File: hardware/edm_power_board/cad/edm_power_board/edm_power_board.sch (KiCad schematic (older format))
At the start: 0 parts

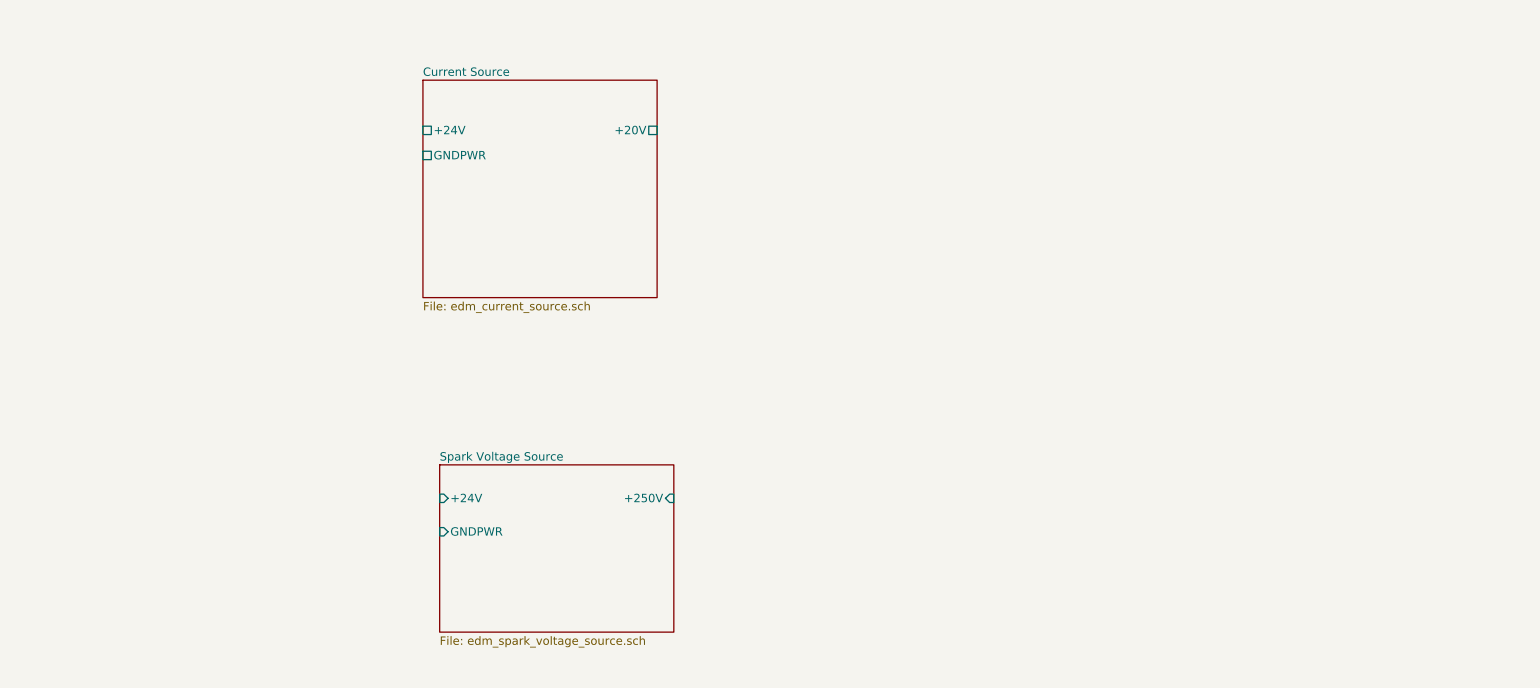
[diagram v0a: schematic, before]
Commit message: Spark voltage source
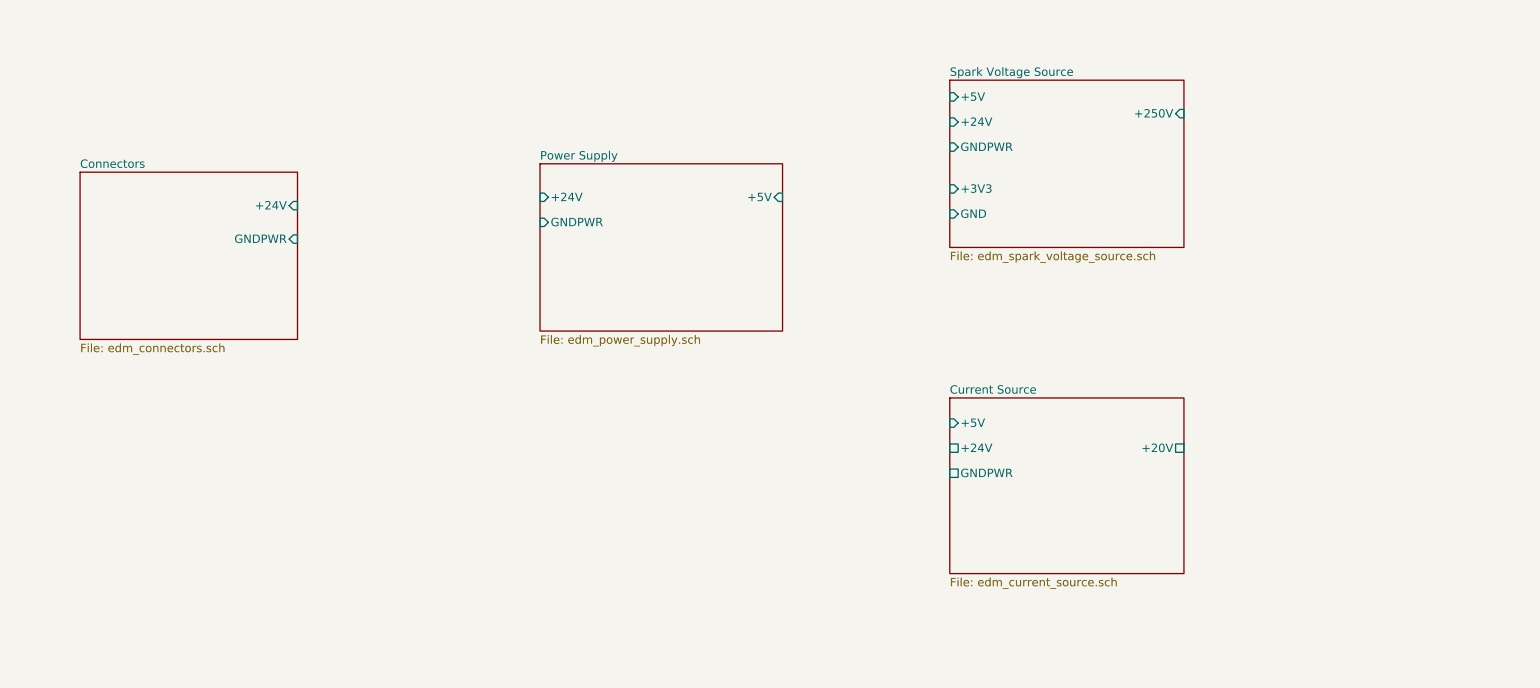
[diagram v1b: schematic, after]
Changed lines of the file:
@@
 $Descr A4 11693 8268
 encoding utf-8
-Sheet 1 3
+Sheet 1 5
 Title ""
 Date ""
@@
 $EndDescr
 $Sheet
-S 3650 2000 1400 1300
+S 6800 3900 1400 1050
 U 5A71F0AB
 F0 "Current Source" 50
 F1 "edm_current_source.sch" 50
-F2 "+24V" U L 3650 2300 50
-F3 "GNDPWR" U L 3650 2450 50
-F4 "+20V" U R 5050 2300 50
+F2 "+24V" U L 6800 4200 50
+F3 "GNDPWR" U L 6800 4350 50
+F4 "+20V" U R 8200 4200 50
+F5 "+5V" I L 6800 4050 50
 $EndSheet
 $Sheet
-S 3750 4300 1400 1000
+S 6800 2000 1400 1000
 U 5A728D61
 F0 "Spark Voltage Source" 50
 F1 "edm_spark_voltage_source.sch" 50
-F2 "+24V" I L 3750 4500 50
-F3 "GNDPWR" I L 3750 4700 50
-F4 "+250V" I R 5150 4500 50
+F2 "+24V" I L 6800 2250 50
+F3 "GNDPWR" I L 6800 2400 50
+F4 "+250V" I R 8200 2200 50
+F5 "+5V" I L 6800 2100 50
+F6 "GND" I L 6800 2800 50
+F7 "+3V3" I L 6800 2650 50
+$EndSheet
+$Sheet
+S 4350 2500 1450 1000
+U 5A73A880
+F0 "Power Supply" 50
+F1 "edm_power_supply.sch" 50
+F2 "+24V" I L 4350 2700 50
+F3 "GNDPWR" I L 4350 2850 50
+F4 "+5V" I R 5800 2700 50
+$EndSheet
+$Sheet
+S 1600 2550 1300 1000
+U 5A73A88E
+F0 "Connectors" 50
+F1 "edm_connectors.sch" 50
+F2 "+24V" I R 2900 2750 50
+F3 "GNDPWR" I R 2900 2950 50
 $EndSheet
 $EndSCHEMATC

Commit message: Insulator
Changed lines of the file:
@@
 $Descr A4 11693 8268
 encoding utf-8
-Sheet 1 5
+Sheet 1 6
 Title ""
 Date ""
@@
 $EndDescr
 $Sheet
-S 6800 3900 1400 1050
+S 5000 3750 1400 400
 U 5A71F0AB
 F0 "Current Source" 50
 F1 "edm_current_source.sch" 50
-F2 "+24V" U L 6800 4200 50
-F3 "GNDPWR" U L 6800 4350 50
-F4 "+20V" U R 8200 4200 50
-F5 "+5V" I L 6800 4050 50
+F2 "+24V" U L 5000 3950 50
+F3 "GNDPWR" U L 5000 4050 50
+F4 "+20V" U R 6400 3850 50
+F5 "+5V" I L 5000 3850 50
 $EndSheet
 $Sheet
-S 6800 2000 1400 1000
+S 5000 2700 1400 600
 U 5A728D61
 F0 "Spark Voltage Source" 50
 F1 "edm_spark_voltage_source.sch" 50
-F2 "+24V" I L 6800 2250 50
-F3 "GNDPWR" I L 6800 2400 50
-F4 "+250V" I R 8200 2200 50
-F5 "+5V" I L 6800 2100 50
-F6 "GND" I L 6800 2800 50
-F7 "+3V3" I L 6800 2650 50
+F2 "+24V" I L 5000 2900 50
+F3 "GNDPWR" I L 5000 3000 50
+F4 "+250V" I R 6400 2800 50
+F5 "+5V" I L 5000 2800 50
+F6 "GND" I L 5000 3200 50
+F7 "+3V3" I L 5000 3100 50
+F8 "Spark_Voltage_0" I R 6400 2900 50
+F9 "Spark_Voltage_1" I R 6400 3000 50
+F10 "Spark_Voltage_2" I R 6400 3100 50
+F11 "Spark_Voltage_Status" I R 6400 3200 50
 $EndSheet
 $Sheet
-S 4350 2500 1450 1000
+S 2900 2700 1200 1000
 U 5A73A880
 F0 "Power Supply" 50
 F1 "edm_power_supply.sch" 50
-F2 "+24V" I L 4350 2700 50
-F3 "GNDPWR" I L 4350 2850 50
-F4 "+5V" I R 5800 2700 50
+F2 "+24V" I L 2900 2900 50
+F3 "GNDPWR" I L 2900 3050 50
+F4 "+5V" I R 4100 2900 50
 $EndSheet
 $Sheet
-S 1600 2550 1300 1000
+S 1200 2700 1200 1000
 U 5A73A88E
 F0 "Connectors" 50
 F1 "edm_connectors.sch" 50
-F2 "+24V" I R 2900 2750 50
-F3 "GNDPWR" I R 2900 2950 50
+F2 "+24V" I R 2400 2900 50
+F3 "GNDPWR" I R 2400 3100 50
+$EndSheet
+$Sheet
+S 7550 2650 1300 800
+U 5A9693D9
+F0 "Spark Output" 50
+F1 "edm_spark_output.sch" 50
 $EndSheet
 $EndSCHEMATC

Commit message: Interconnections
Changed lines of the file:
@@
 $EndDescr
 $Sheet
-S 5000 3750 1400 400
+S 5050 5050 1400 400
 U 5A71F0AB
 F0 "Current Source" 50
 F1 "edm_current_source.sch" 50
-F2 "+24V" U L 5000 3950 50
-F3 "GNDPWR" U L 5000 4050 50
-F4 "+20V" U R 6400 3850 50
-F5 "+5V" I L 5000 3850 50
-$EndSheet
-$Sheet
-S 5000 2700 1400 600
+F2 "+24V" U L 5050 5250 50
+F3 "GNDPWR" U L 5050 5350 50
+F4 "+20V" U R 6450 5150 50
+F5 "+5V" I L 5050 5150 50
+$EndSheet
+$Sheet
+S 5050 3550 1400 600
 U 5A728D61
 F0 "Spark Voltage Source" 50
 F1 "edm_spark_voltage_source.sch" 50
-F2 "+24V" I L 5000 2900 50
-F3 "GNDPWR" I L 5000 3000 50
-F4 "+250V" I R 6400 2800 50
-F5 "+5V" I L 5000 2800 50
-F6 "GND" I L 5000 3200 50
-F7 "+3V3" I L 5000 3100 50
-F8 "Spark_Voltage_0" I R 6400 2900 50
-F9 "Spark_Voltage_1" I R 6400 3000 50
-F10 "Spark_Voltage_2" I R 6400 3100 50
-F11 "Spark_Voltage_Status" I R 6400 3200 50
-$EndSheet
-$Sheet
-S 2900 2700 1200 1000
+F2 "+24V" I L 5050 3750 50
+F3 "GNDPWR" I L 5050 3850 50
+F4 "+250V" I R 6450 3650 50
+F5 "+5V" I L 5050 3650 50
+F6 "GND" I L 5050 4050 50
+F7 "+3V3" I L 5050 3950 50
+F8 "Spark_Voltage_0" I R 6450 3750 50
+F9 "Spark_Voltage_1" I R 6450 3850 50
+F10 "Spark_Voltage_2" I R 6450 3950 50
+F11 "Spark_Voltage_Status" I R 6450 4050 50
+$EndSheet
+$Sheet
+S 1950 3550 1400 750
 U 5A73A880
 F0 "Power Supply" 50
 F1 "edm_power_supply.sch" 50
-F2 "+24V" I L 2900 2900 50
-F3 "GNDPWR" I L 2900 3050 50
-F4 "+5V" I R 4100 2900 50
-$EndSheet
-$Sheet
-S 1200 2700 1200 1000
+F2 "+24V" I L 1950 3650 50
+F3 "GNDPWR" I L 1950 3750 50
+F4 "+5V" I R 3350 3650 50
+$EndSheet
+$Sheet
+S 5050 1700 1400 900
 U 5A73A88E
 F0 "Connectors" 50
 F1 "edm_connectors.sch" 50
-F2 "+24V" I R 2400 2900 50
-F3 "GNDPWR" I R 2400 3100 50
-$EndSheet
-$Sheet
-S 7550 2650 1300 800
+F2 "+24V" I L 5050 1800 50
+F3 "GNDPWR" I L 5050 1900 50
+F4 "Output_250V_Enable" I R 6450 1800 50
+F5 "Output_20V_Enable" I R 6450 1900 50
+F6 "Short_Circuit" I R 6450 2000 50
+F7 "Breakdown" I R 6450 2100 50
+F8 "Spark_Voltage_0" I R 6450 2200 50
+F9 "Spark_Voltage_1" I R 6450 2300 50
+F10 "Spark_Voltage_2" I R 6450 2400 50
+F11 "Spark_Voltage_Status" I R 6450 2500 50
+F12 "+3V3" I L 5050 2100 50
+F13 "GND" I L 5050 2200 50
+$EndSheet
+$Sheet
+S 8250 3550 1300 700
 U 5A9693D9
 F0 "Spark Output" 50
 F1 "edm_spark_output.sch" 50
-$EndSheet
+F2 "+250V" I L 8250 3650 50
+F3 "+20V" I L 8250 3750 50
+F4 "+5V" I L 8250 4050 50
+F5 "+3V3" I L 8250 3850 50
+F6 "GND" I L 8250 3950 50
+F7 "GNDPWR" I L 8250 4150 50
+F8 "Output_250V_Enable" I R 9550 3650 50
+F9 "Output_20V_Enable" I R 9550 3750 50
+F10 "Short_Circuit" I R 9550 3850 50
+F11 "Breakdown" I R 9550 3950 50
+$EndSheet
+Wire Wire Line
+	6450 3650 8250 3650
+Wire Wire Line
+	6450 5150 7400 5150
+Wire Wire Line
+	7400 5150 7400 3750
+Wire Wire Line
+	7400 3750 8250 3750
+Wire Wire Line
+	6450 3750 6700 3750
+Wire Wire Line
+	6700 3750 6700 2200
+Wire Wire Line
+	6700 2200 6450 2200
+Wire Wire Line
+	6450 2300 6800 2300
+Wire Wire Line
+	6800 2300 6800 3850
+Wire Wire Line
+	6800 3850 6450 3850
+Wire Wire Line
+	6450 3950 6900 3950
+Wire Wire Line
+	6900 3950 6900 2400
+Wire Wire Line
+	6900 2400 6450 2400
+Wire Wire Line
+	6450 2500 7000 2500
+Wire Wire Line
+	7000 2500 7000 4050
+Wire Wire Line
+	7000 4050 6450 4050
+Wire Wire Line
+	6450 2100 10200 2100
+Wire Wire Line
+	10200 2100 10200 3950
+Wire Wire Line
+	10200 3950 9550 3950
+Wire Wire Line
+	6450 2000 10100 2000
+Wire Wire Line
+	10100 2000 10100 3850
+Wire Wire Line
+	10100 3850 9550 3850
+Wire Wire Line
+	9550 3750 10000 3750
+Wire Wire Line
+	10000 3750 10000 1900
+Wire Wire Line
+	10000 1900 6450 1900
+Wire Wire Line
+	6450 1800 9900 1800
+Wire Wire Line
+	9900 1800 9900 3650
+Wire Wire Line
+	9900 3650 9550 3650
+Wire Wire Line
+	3350 3650 4150 3650
+Wire Wire Line
+	5050 5150 4700 5150
+Wire Wire Line
+	4150 5150 4150 3650
+Connection ~ 4150 3650
+Wire Wire Line
+	4150 3650 5050 3650
+Wire Wire Line
+	5050 5250 4250 5250
+Wire Wire Line
+	4250 5250 4250 3750
+Wire Wire Line
+	4250 3750 5050 3750
+Wire Wire Line
+	5050 3850 4350 3850
+Wire Wire Line
+	4350 3850 4350 5350
+Wire Wire Line
+	4350 5350 4800 5350
+Wire Wire Line
+	5050 3950 4600 3950
+Wire Wire Line
+	4600 3950 4600 2100
+Wire Wire Line
+	4600 2100 5050 2100
+Wire Wire Line
+	5050 4050 4700 4050
+Wire Wire Line
+	4700 4050 4700 2200
+Wire Wire Line
+	4700 2200 5050 2200
+Wire Wire Line
+	7750 4450 4600 4450
+Wire Wire Line
+	4600 4450 4600 3950
+Connection ~ 4600 3950
+Wire Wire Line
+	7850 4550 4700 4550
+Wire Wire Line
+	4700 4550 4700 4050
+Connection ~ 4700 4050
+Wire Wire Line
+	4350 5350 1700 5350
+Wire Wire Line
+	1700 5350 1700 3750
+Wire Wire Line
+	1700 3750 1950 3750
+Connection ~ 4350 5350
+Wire Wire Line
+	1950 3650 1600 3650
+Wire Wire Line
+	1600 3650 1600 5250
+Wire Wire Line
+	1600 5250 4250 5250
+Connection ~ 4250 5250
+Wire Wire Line
+	4800 5350 4800 4750
+Connection ~ 4800 5350
+Wire Wire Line
+	4800 5350 5050 5350
+Wire Wire Line
+	4700 4650 4700 5150
+Connection ~ 4700 5150
+Wire Wire Line
+	4700 5150 4150 5150
+Wire Wire Line
+	7750 4450 7750 3850
+Wire Wire Line
+	7750 3850 8250 3850
+Wire Wire Line
+	8250 3950 7850 3950
+Wire Wire Line
+	7850 3950 7850 4550
+Wire Wire Line
+	8250 4050 7950 4050
+Wire Wire Line
+	7950 4050 7950 4650
+Wire Wire Line
+	4700 4650 7950 4650
+Wire Wire Line
+	8050 4750 8050 4150
+Wire Wire Line
+	8050 4150 8250 4150
+Wire Wire Line
+	4800 4750 8050 4750
+Wire Wire Line
+	1700 3750 1700 1900
+Wire Wire Line
+	1700 1900 5050 1900
+Connection ~ 1700 3750
+Wire Wire Line
+	5050 1800 1600 1800
+Wire Wire Line
+	1600 1800 1600 3650
+Connection ~ 1600 3650
 $EndSCHEMATC

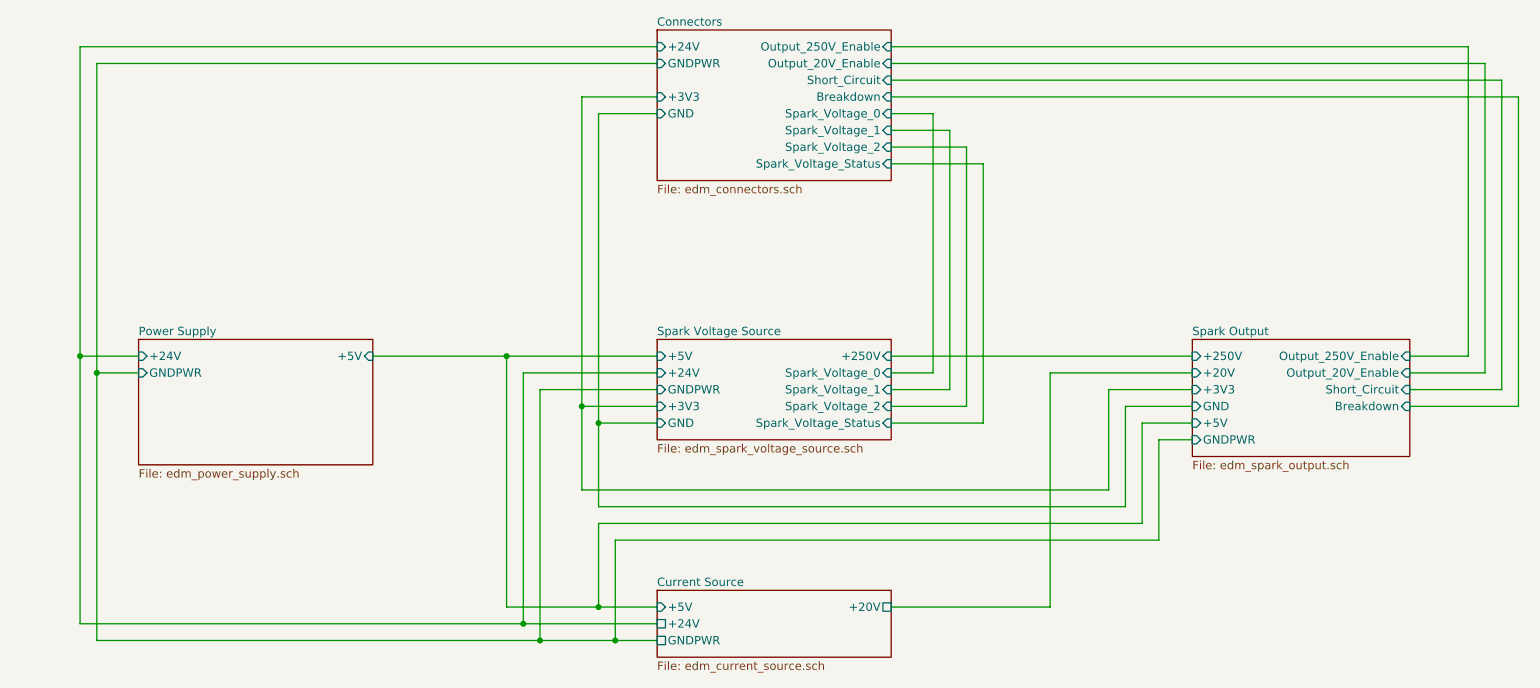
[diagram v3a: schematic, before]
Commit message: Spark output connector
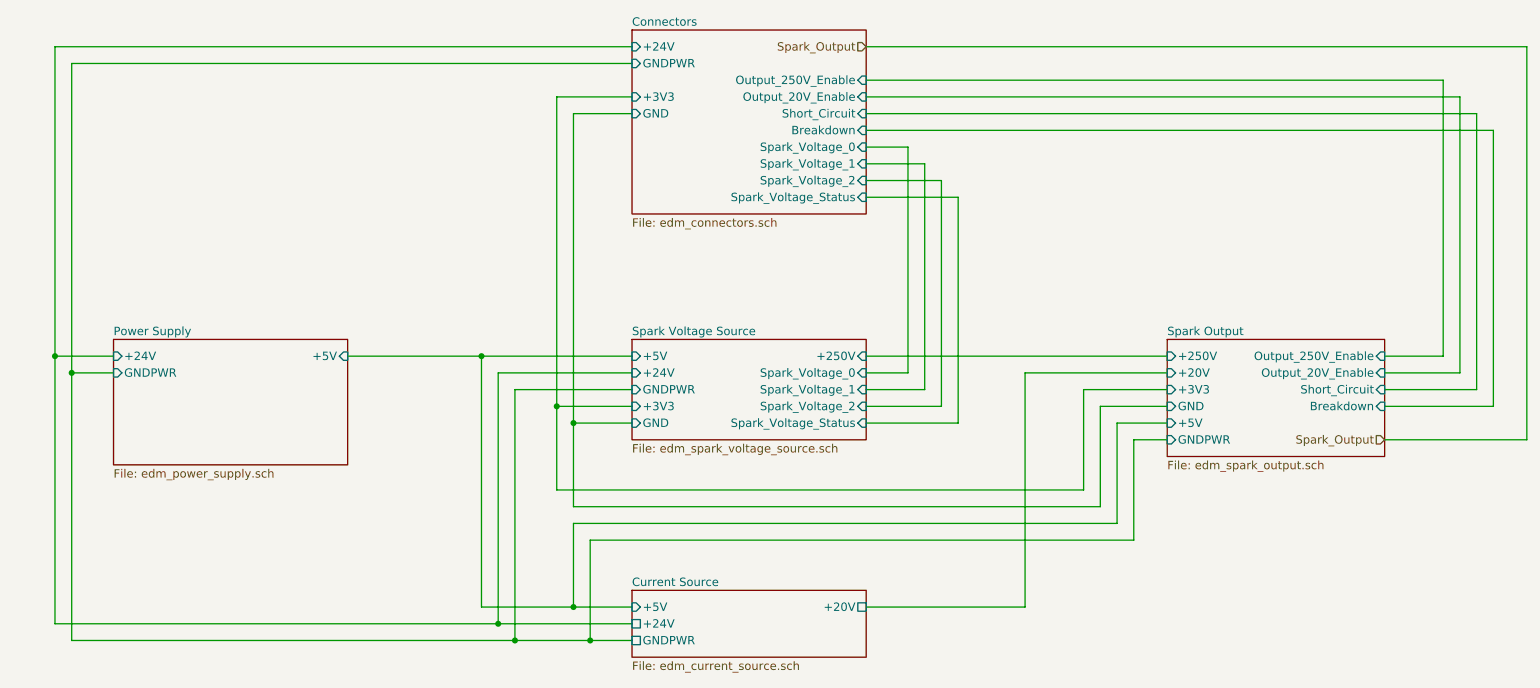
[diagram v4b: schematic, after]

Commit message: Component placement
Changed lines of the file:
@@
 F12 "+3V3" I L 4900 2100 50
 F13 "GND" I L 4900 2200 50
+F14 "Spark_Output" I R 6300 1800 50
 $EndSheet
 $Sheet
@@
 F10 "Short_Circuit" I R 9400 3850 50
 F11 "Breakdown" I R 9400 3950 50
+F12 "Spark_Output" I R 9400 4150 50
 $EndSheet
 Wire Wire Line
@@
 	1450 1800 1450 3650
 Connection ~ 1450 3650
-Text HLabel 9400 4150 0    50   Input ~ 0
-Spark_Output
-Text HLabel 6300 1800 0    50   Input ~ 0
-Spark_Output
 Wire Wire Line
-	6300 1800 10250 1800
+	9400 4150 10250 4150
 Wire Wire Line
-	10250 1800 10250 4150
+	10250 4150 10250 1800
 Wire Wire Line
-	10250 4150 9400 4150
+	10250 1800 6300 1800
 $EndSCHEMATC
